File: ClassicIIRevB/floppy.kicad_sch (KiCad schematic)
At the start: 20 parts, among them J5 EXT FLOPPY, J9 INT FLOPPY, U9 SWIM

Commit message: improved footprints and silkscreens
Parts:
- RC3: footprint Package_SO:SOIC-20W_7.5x12.8mm_P1.27mm -> MyPackage:SOIC-20W_7.5x12.8mm_P1.27mm_oval
- U9: footprint Package_LCC:PLCC-44_16.6x16.6mm_P1.27mm -> MyPackage:PLCC-44_16.6x16.6mm_P1.27mm_oval
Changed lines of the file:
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@@
 	(title_block
 		(title "Macintosh Classic II Revision B")
-		(date "2025-05-31")
+		(date "2025-06-04")
 		(company "Apple Computer")
 		(comment 1 "drawn by Bradley Bell")
@@
 			)
 		)
-		(property "Footprint" "Package_LCC:PLCC-44_16.6x16.6mm_P1.27mm"
+		(property "Footprint" "MyPackage:PLCC-44_16.6x16.6mm_P1.27mm_oval"
 			(at 73.66 142.24 0)
 			(effects
@@
 			)
 		)
-		(property "Footprint" "Package_SO:SOIC-20W_7.5x12.8mm_P1.27mm"
+		(property "Footprint" "MyPackage:SOIC-20W_7.5x12.8mm_P1.27mm_oval"
 			(at 147.32 106.68 0)
 			(effects

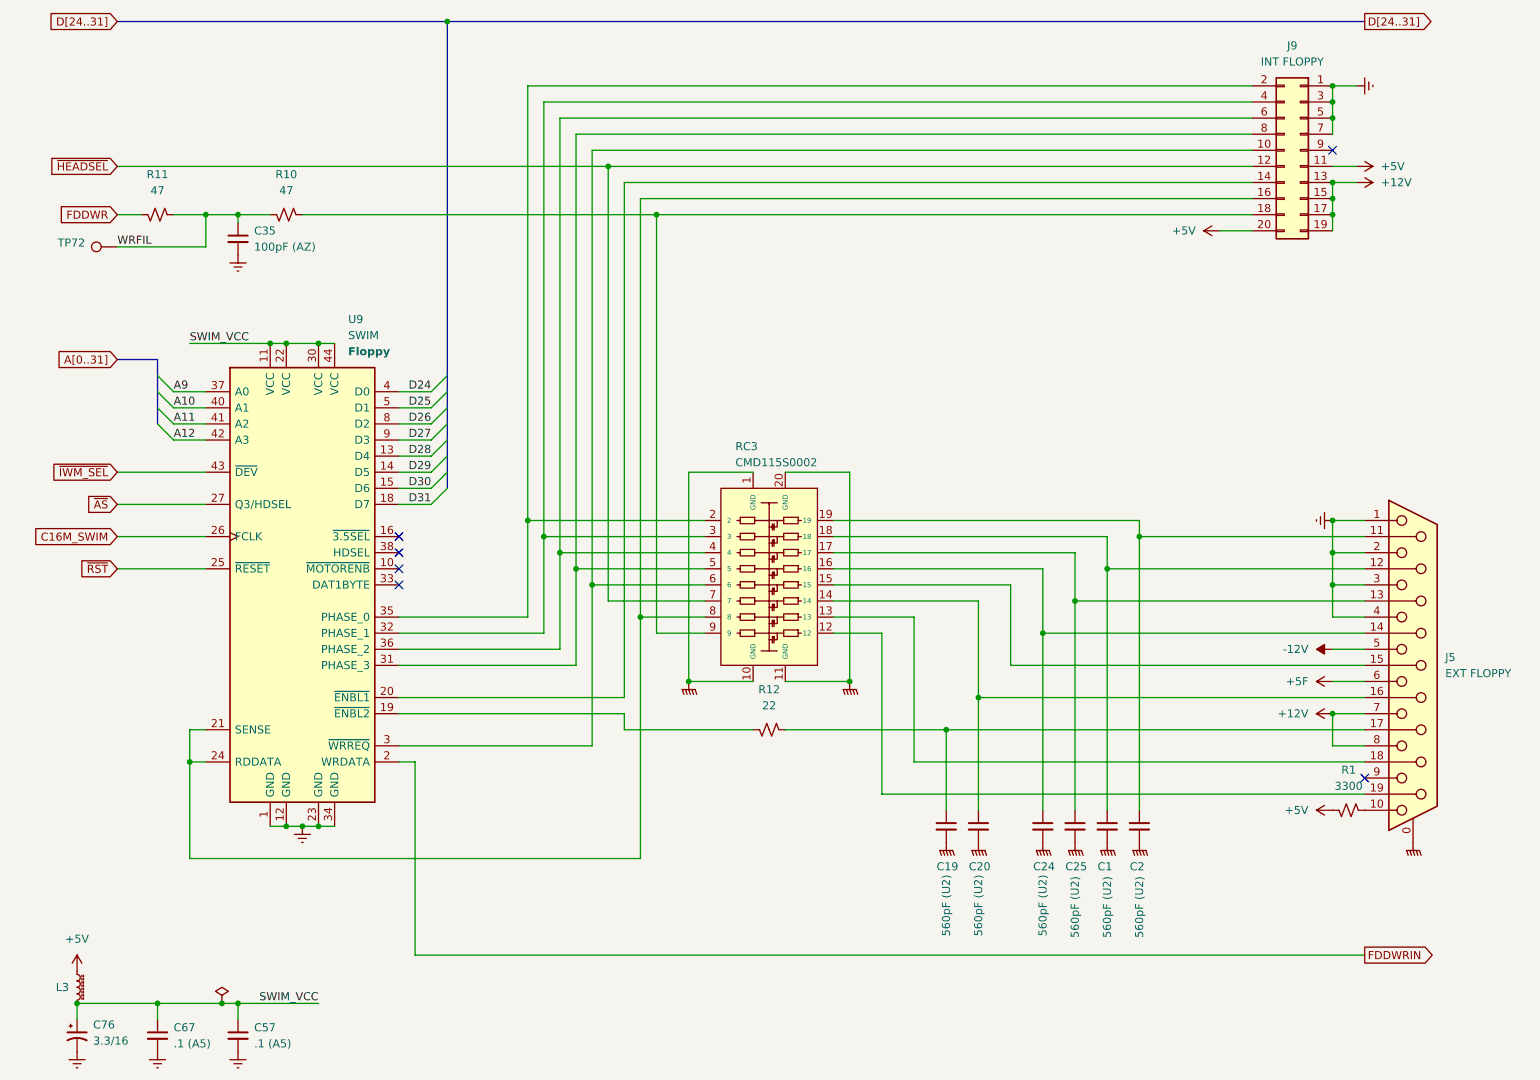
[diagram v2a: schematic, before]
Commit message: Switch to some "official" net names
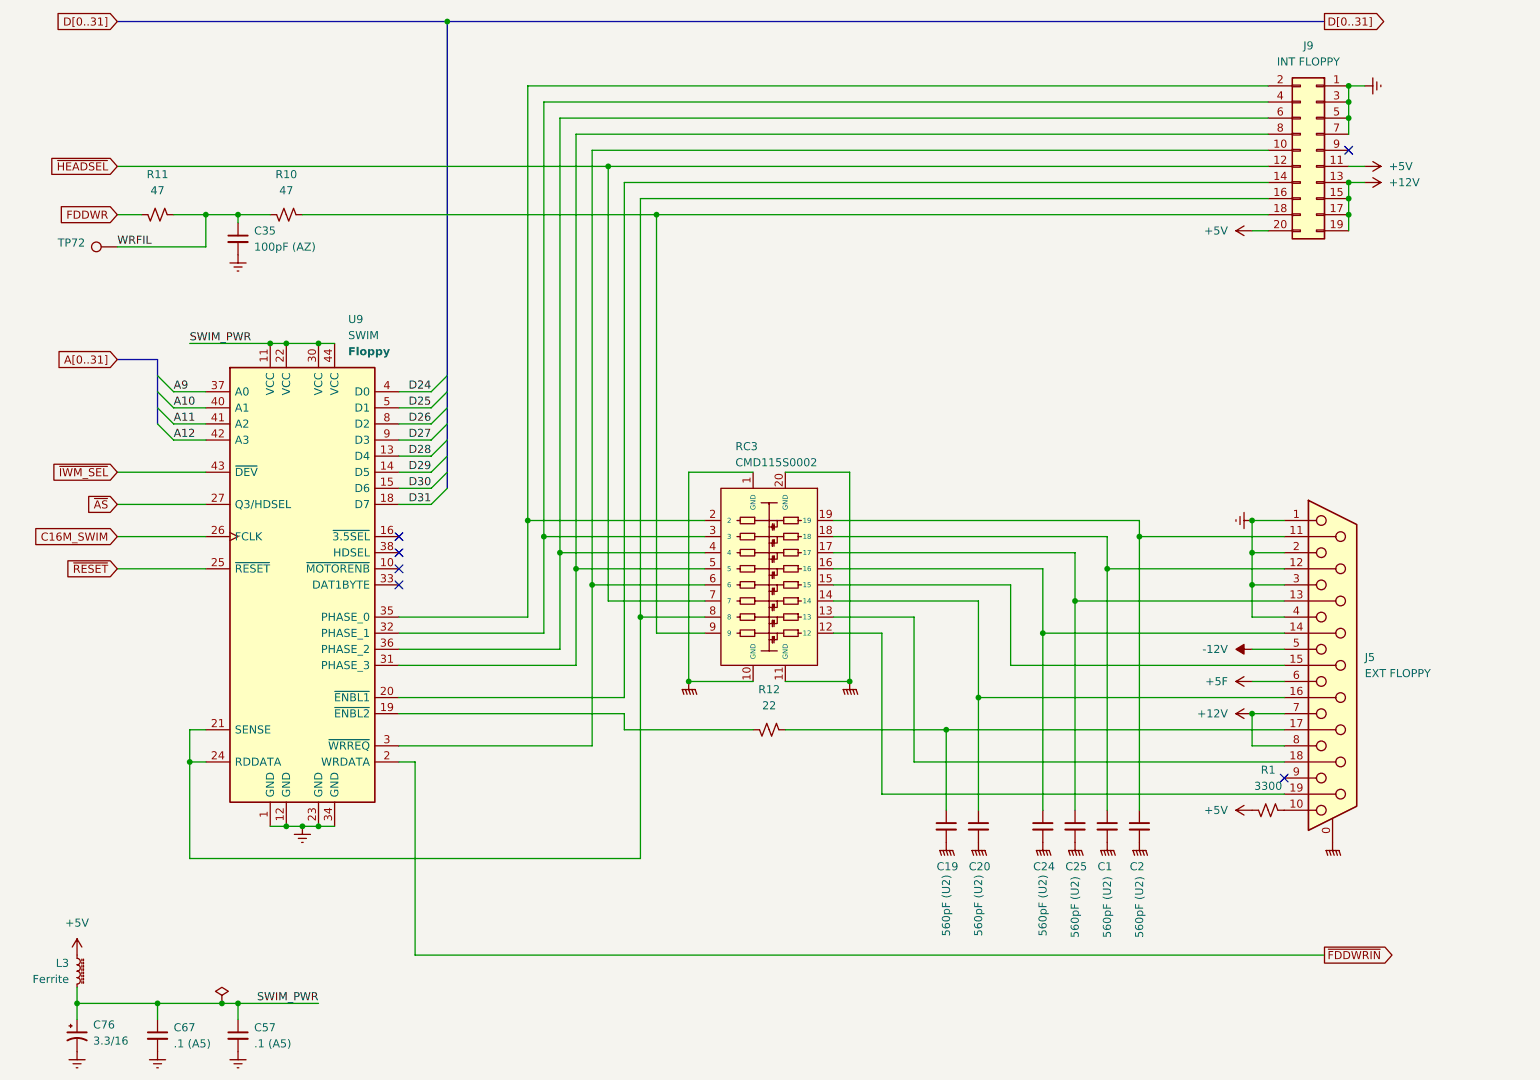
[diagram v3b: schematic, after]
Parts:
- L3: value L_Ferrite_Small -> Ferrite
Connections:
- net FDDWRIN renamed ~{FDDWRIN}
- net SWIM_VCC renamed SWIM_PWR
- net ~{RST} renamed ~{RESET}
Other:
- moved on the sheet: J5, J9, L3, R1

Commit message: update exports
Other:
- title: Macintosh Classic II Revision B -> Macintosh Classic II (Later Revision)
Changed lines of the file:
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@@
 	(paper "USLetter")
 	(title_block
-		(title "Macintosh Classic II Revision B")
-		(date "2025-06-04")
+		(title "Macintosh Classic II (Later Revision)")
+		(date "2025-06-16")
 		(company "Apple Computer")
 		(comment 1 "drawn by Bradley Bell")

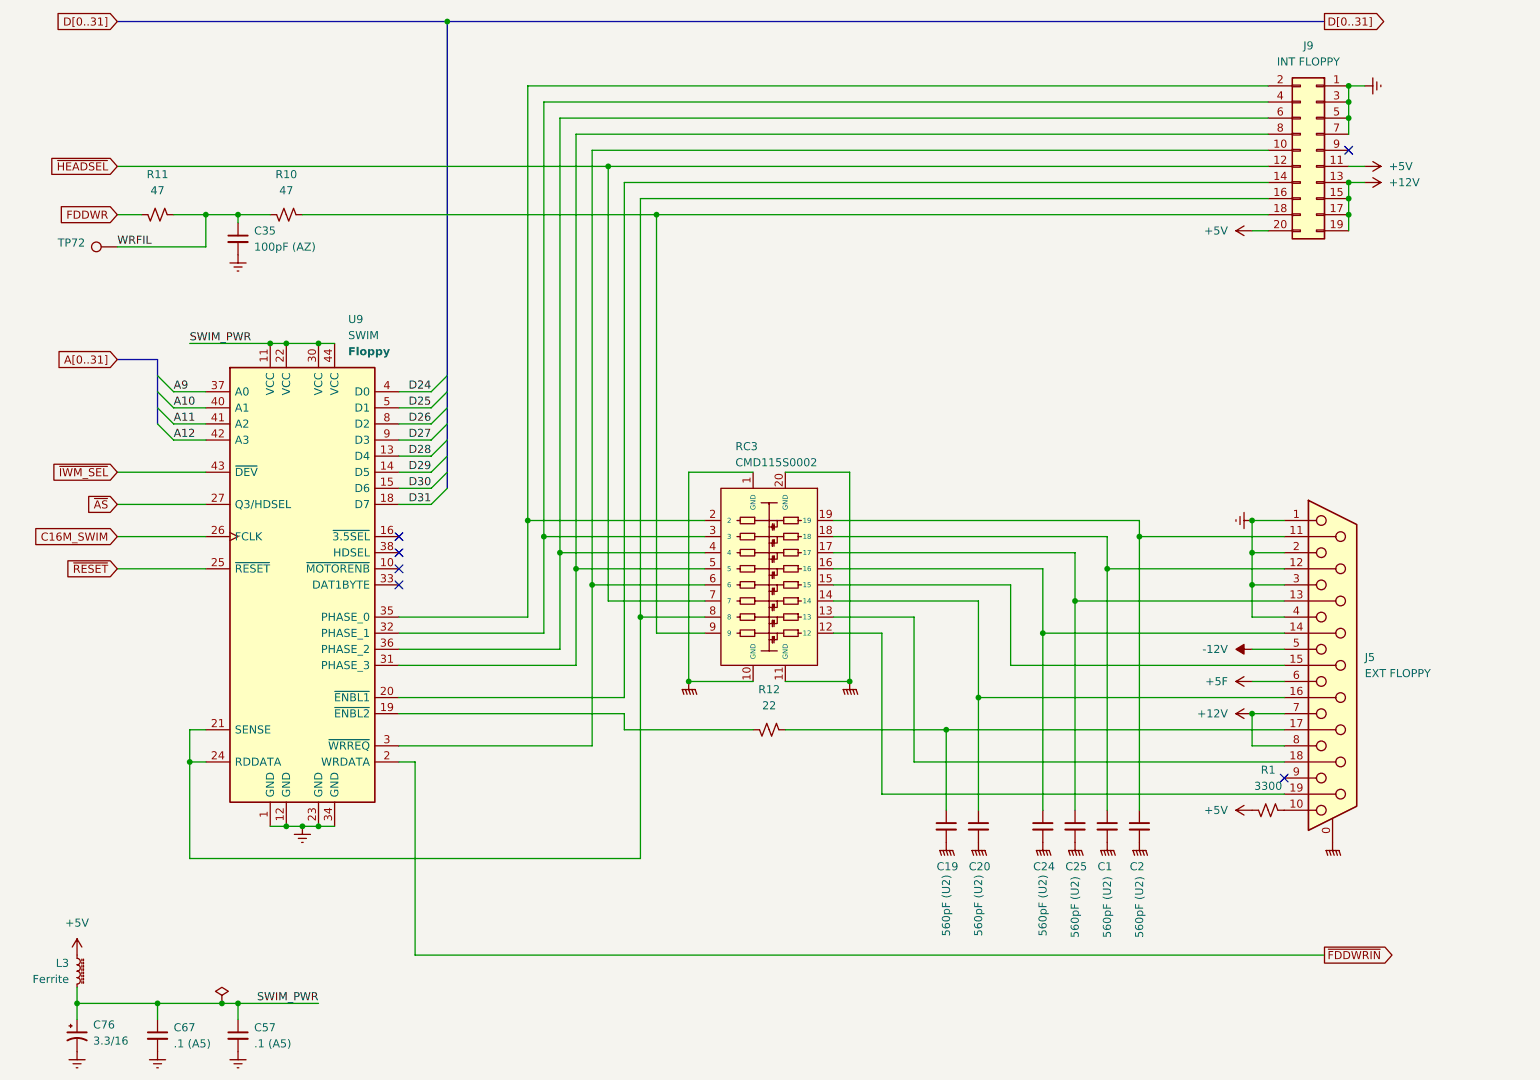
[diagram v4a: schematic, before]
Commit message: Corrections to SMDs, more improved footprints
The later revision board reproduction design is now complete.
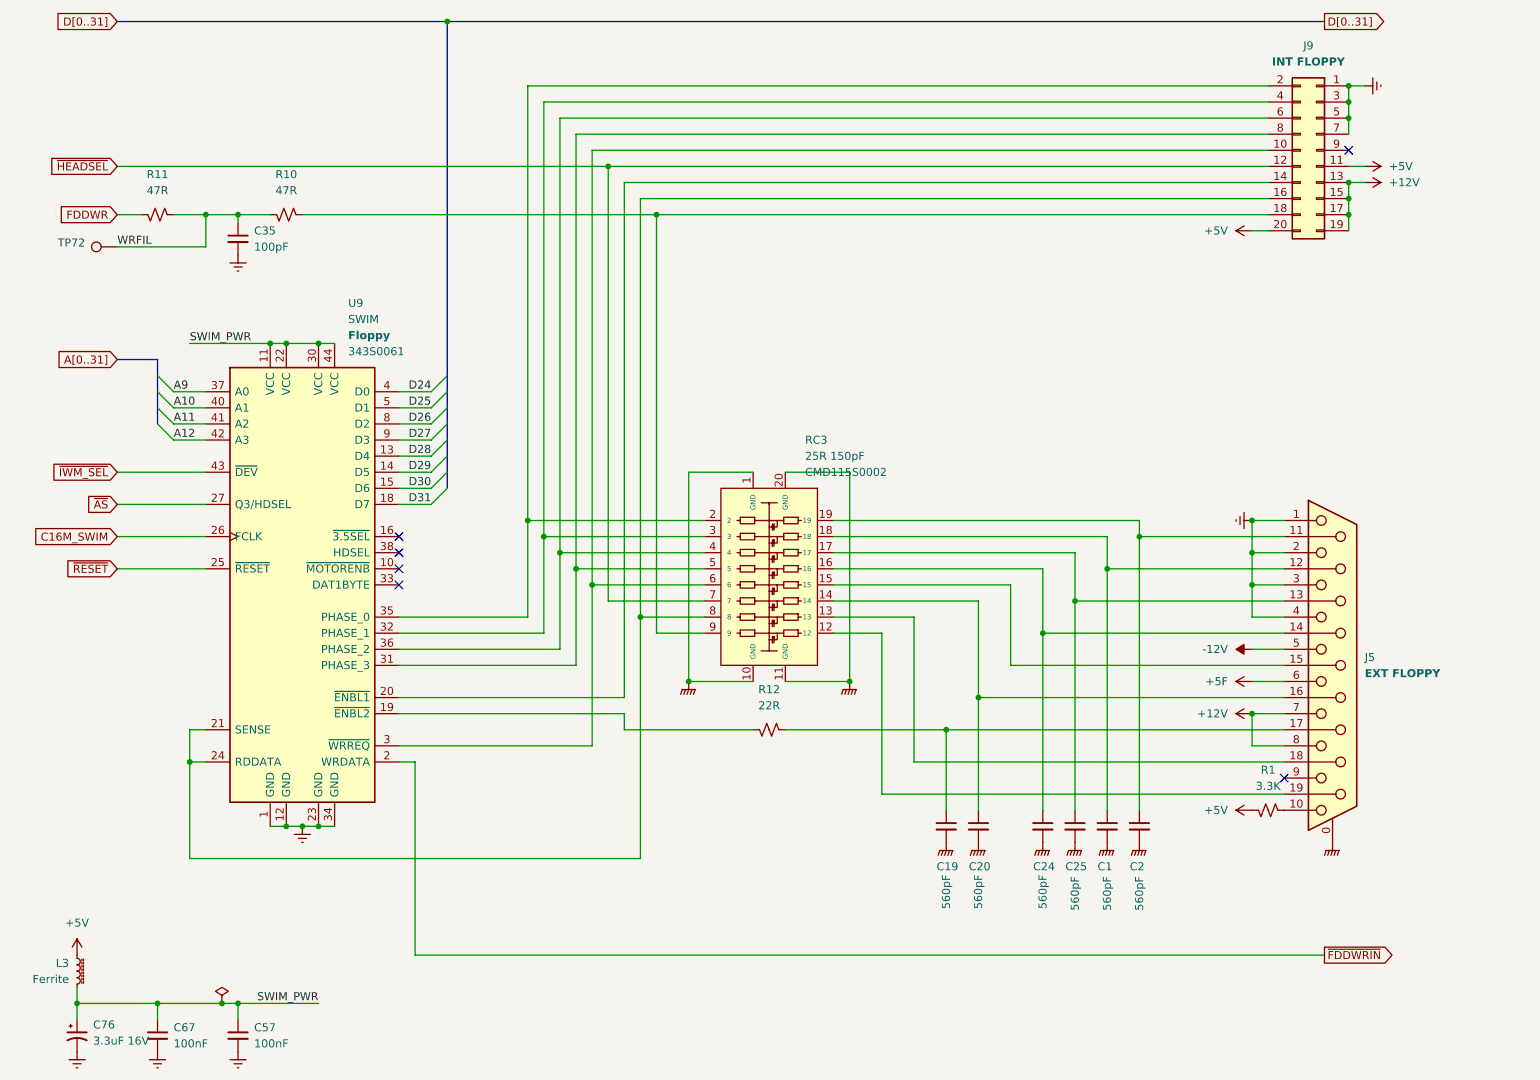
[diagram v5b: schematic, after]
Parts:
- C1, C19, C2, C20, C24, C25: value 560pF (U2) -> 560pF
- C35: value 100pF (AZ) -> 100pF
- C57, C67: value .1 (A5) -> 100nF
- C76: value 3.3/16 -> 3.3uF 16V
- J9: footprint Connector_IDC:IDC-Header_2x10_P2.54mm_Vertical -> Connector_Mine:IDC-Header_2x10_P2.54mm_Vertical
- R1: value 3300 -> 3.3K
- R10, R11: value 47 -> 47R
- R12: value 22 -> 22R
- RC3: value CMD115S0002 -> 25R 150pF; PartNum (none) -> CMD115S0002
- TP72: now left out of the parts list
- U9: PartNum (none) -> 343S0061
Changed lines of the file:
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@@
 	(title_block
 		(title "Macintosh Classic II (Later Revision)")
-		(date "2025-06-16")
+		(date "2025-06-21")
 		(company "Apple Computer")
 		(comment 1 "drawn by Bradley Bell")
@@
 			)
 		)
-		(property "Value" ".1 (A5)"
+		(property "Value" "100nF"
 			(at 66.04 181.6162 0)
 			(effects
@@
 		(lib_id "power:GNDPWR")
 		(at 180.34 149.86 0)
-		(mirror y)
 		(unit 1)
 		(exclude_from_sim no)
@@
 		(on_board yes)
 		(dnp no)
-		(fields_autoplaced yes)
 		(property "Reference" "#PWR095"
 			(at 180.34 154.94 0)
@@
 		)
 		(property "Value" "GNDPWR"
-			(at 180.467 153.67 0)
+			(at 180.213 153.67 0)
 			(effects
 				(font
@@
 		(lib_id "power:GNDPWR")
 		(at 160.02 124.46 0)
-		(mirror y)
 		(unit 1)
 		(exclude_from_sim no)
@@
 		(on_board yes)
 		(dnp no)
-		(fields_autoplaced yes)
 		(property "Reference" "#PWR0177"
 			(at 160.02 129.54 0)
@@
 		)
 		(property "Value" "GNDPWR"
-			(at 160.147 128.27 0)
+			(at 159.893 128.27 0)
 			(effects
 				(font
@@
 		(lib_id "power:GNDPWR")
 		(at 134.62 124.46 0)
-		(mirror y)
 		(unit 1)
 		(exclude_from_sim no)
@@
 		(on_board yes)
 		(dnp no)
-		(fields_autoplaced yes)
 		(property "Reference" "#PWR0248"
 			(at 134.62 129.54 0)
@@
 		)
 		(property "Value" "GNDPWR"
-			(at 134.747 128.27 0)
+			(at 134.493 128.27 0)
 			(effects
 				(font
@@
 		(lib_id "power:GNDPWR")
 		(at 205.74 149.86 0)
-		(mirror y)
 		(unit 1)
 		(exclude_from_sim no)
@@
 		(on_board yes)
 		(dnp no)
-		(fields_autoplaced yes)
 		(property "Reference" "#PWR063"
 			(at 205.74 154.94 0)
@@
 		)
 		(property "Value" "GNDPWR"
-			(at 205.867 153.67 0)
+			(at 205.613 153.67 0)
 			(effects
 				(font
@@
 			)
 		)
-		(property "Value" "3300"
+		(property "Value" "3.3K"
 			(at 226.06 140.97 90)
 			(effects
@@
 			)
 		)
-		(property "Value" "560pF (U2)"
+		(property "Value" "560pF"
 			(at 180.34 154.94 90)
 			(effects
@@
 		(fields_autoplaced yes)
 		(property "Reference" "U9"
-			(at 80.8833 67.31 0)
+			(at 80.8833 64.77 0)
 			(effects
 				(font
@@
 		)
 		(property "Value" "SWIM"
-			(at 80.8833 69.85 0)
+			(at 80.8833 67.31 0)
 			(effects
 				(font
@@
 		)
 		(property "Description" "Floppy"
-			(at 80.8833 72.39 0)
+			(at 80.8833 69.85 0)
 			(effects
 				(font
@@
 			)
 		)
+		(property "PartNum" "343S0061"
+			(at 80.8833 72.39 0)
+			(effects
+				(font
+					(size 1.27 1.27)
+				)
+				(justify left)
+			)
+		)
 		(pin "14"
 		)
@@
 			)
 		)
-		(property "Value" "3.3/16"
+		(property "Value" "3.3uF 16V"
 			(at 40.64 181.1781 0)
 			(effects
@@
 				(font
 					(size 1.27 1.27)
+					(thickness 0.254)
+					(bold yes)
 				)
 			)
 		)
-		(property "Footprint" "Connector_IDC:IDC-Header_2x10_P2.54mm_Vertical"
+		(property "Footprint" "Connector_Mine:IDC-Header_2x10_P2.54mm_Vertical"
 			(at 233.68 40.64 0)
 			(effects
@@
 			)
 		)
-		(property "Value" "560pF (U2)"
+		(property "Value" "560pF"
 			(at 190.5 154.94 90)
 			(effects
@@
 		(lib_id "power:GNDPWR")
 		(at 236.22 149.86 0)
-		(mirror y)
 		(unit 1)
 		(exclude_from_sim no)
@@
 		(on_board yes)
 		(dnp no)
-		(fields_autoplaced yes)
 		(property "Reference" "#PWR0123"
 			(at 236.22 154.94 0)
@@
 		)
 		(property "Value" "GNDPWR"
-			(at 236.347 153.67 0)
+			(at 236.093 153.67 0)
 			(effects
 				(font
@@
 			)
 		)
-		(property "Value" "560pF (U2)"
+		(property "Value" "560pF"
 			(at 175.26 154.94 90)
 			(effects
@@
 			)
 		)
-		(property "Value" "560pF (U2)"
+		(property "Value" "560pF"
 			(at 195.58 155.194 90)
 			(effects
@@
 			)
 		)
-		(property "Value" "47"
+		(property "Value" "47R"
 			(at 71.12 46.99 90)
 			(effects
@@
 			)
 		)
-		(property "Value" "100pF (AZ)"
+		(property "Value" "100pF"
 			(at 66.04 55.8862 0)
 			(effects
@@
 		)
 		(property "Value" "EXT FLOPPY"
-			(at 241.3 123.1899 0)
+			(at 241.3 123.19 0)
 			(effects
 				(font
 					(size 1.27 1.27)
+					(thickness 0.254)
+					(bold yes)
 				)
 				(justify left)
@@
 			)
 		)
-		(property "Value" "560pF (U2)"
+		(property "Value" "560pF"
 			(at 200.66 155.194 90)
 			(effects
@@
 			)
 		)
-		(property "Value" ".1 (A5)"
+		(property "Value" "100nF"
 			(at 53.34 181.6162 0)
 			(effects
@@
 		(on_board yes)
 		(dnp no)
+		(fields_autoplaced yes)
 		(property "Reference" "RC3"
-			(at 141.986 87.376 90)
+			(at 152.9781 86.36 90)
 			(effects
 				(font
@@
 			)
 		)
-		(property "Value" "CMD115S0002"
-			(at 141.986 89.916 90)
+		(property "Value" "25R 150pF"
+			(at 152.9781 88.9 90)
 			(effects
 				(font
@@
 			)
 		)
+		(property "PartNum" "CMD115S0002"
+			(at 152.9781 91.44 90)
+			(effects
+				(font
+					(size 1.27 1.27)
+				)
+				(justify left)
+			)
+		)
 		(pin "1"
 		)
@@
 		(lib_id "power:GNDPWR")
 		(at 195.58 149.86 0)
-		(mirror y)
 		(unit 1)
 		(exclude_from_sim no)
@@
 		(on_board yes)
 		(dnp no)
-		(fields_autoplaced yes)
 		(property "Reference" "#PWR065"
 			(at 195.58 154.94 0)
@@
 		)
 		(property "Value" "GNDPWR"
-			(at 195.707 153.67 0)
+			(at 195.453 153.67 0)
 			(effects
 				(font
@@
 			)
 		)
-		(property "Value" "22"
+		(property "Value" "22R"
 			(at 147.32 128.27 90)
 			(effects
@@
 		(lib_id "power:GNDPWR")
 		(at 190.5 149.86 0)
-		(mirror y)
 		(unit 1)
 		(exclude_from_sim no)
@@
 		(on_board yes)
 		(dnp no)
-		(fields_autoplaced yes)
 		(property "Reference" "#PWR067"
 			(at 190.5 154.94 0)
@@
 		)
 		(property "Value" "GNDPWR"
-			(at 190.627 153.67 0)
+			(at 190.373 153.67 0)
 			(effects
 				(font
@@
 			)
 		)
-		(property "Value" "560pF (U2)"
+		(property "Value" "560pF"
 			(at 205.74 155.194 90)
 			(effects
@@
 			)
 		)
-		(property "Value" "47"
+		(property "Value" "47R"
 			(at 50.8 46.99 90)
 			(effects
@@
 		(lib_id "power:GNDPWR")
 		(at 200.66 149.86 0)
-		(mirror y)
 		(unit 1)
 		(exclude_from_sim no)
@@
 		(on_board yes)
 		(dnp no)
-		(fields_autoplaced yes)
 		(property "Reference" "#PWR064"
 			(at 200.66 154.94 0)
@@
 		)
 		(property "Value" "GNDPWR"
-			(at 200.787 153.67 0)
+			(at 200.533 153.67 0)
 			(effects
 				(font
@@
 		(unit 1)
 		(exclude_from_sim no)
-		(in_bom yes)
+		(in_bom no)
 		(on_board yes)
 		(dnp no)
@@
 		(lib_id "power:GNDPWR")
 		(at 175.26 149.86 0)
-		(mirror y)
 		(unit 1)
 		(exclude_from_sim no)
@@
 		(on_board yes)
 		(dnp no)
-		(fields_autoplaced yes)
 		(property "Reference" "#PWR0102"
 			(at 175.26 154.94 0)
@@
 		)
 		(property "Value" "GNDPWR"
-			(at 175.387 153.67 0)
+			(at 175.133 153.67 0)
 			(effects
 				(font
